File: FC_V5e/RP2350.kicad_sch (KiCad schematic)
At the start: 34 parts, among them U11 W25Q128JVS, U18 RP2350_60QFN, U5 APS1604M-3SQR-SN_C18214056, Y1 ABM8-272-T3

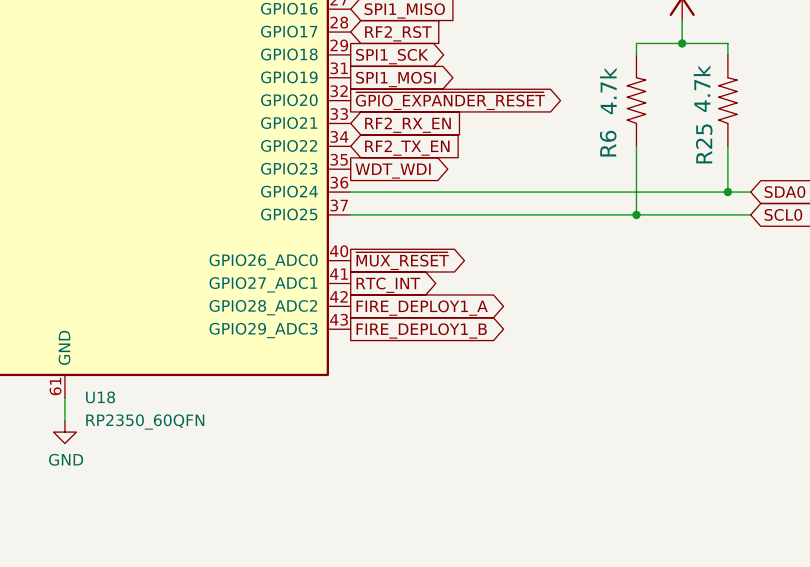
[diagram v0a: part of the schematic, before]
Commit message: Added RV3032 to Schematic
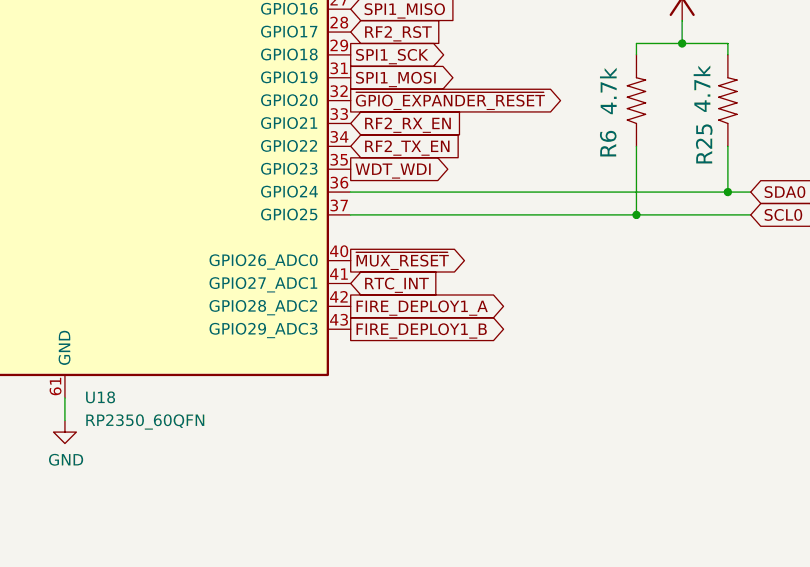
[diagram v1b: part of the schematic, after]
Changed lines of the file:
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@@
 	)
 	(global_label "RTC_INT"
-		(shape output)
+		(shape input)
 		(at 209.55 143.51 0)
 		(fields_autoplaced yes)

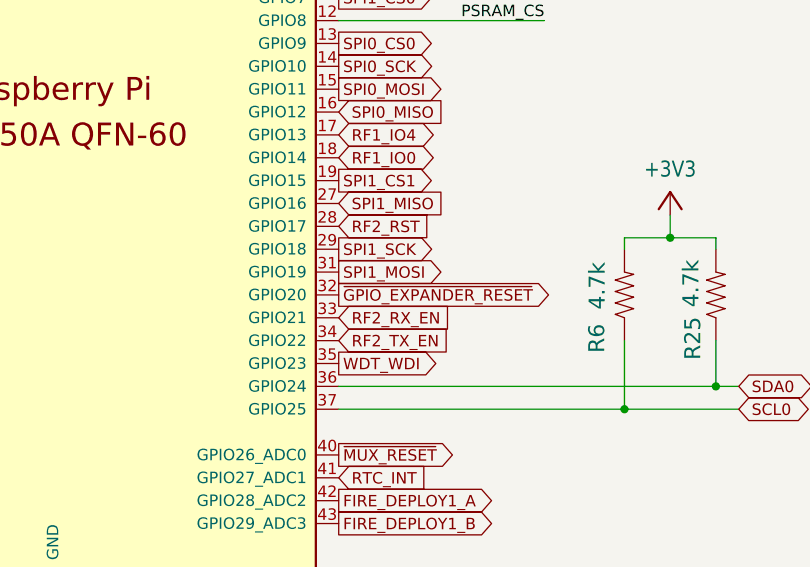
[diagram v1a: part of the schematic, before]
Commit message: Removed RF2: E28-2G4M27S
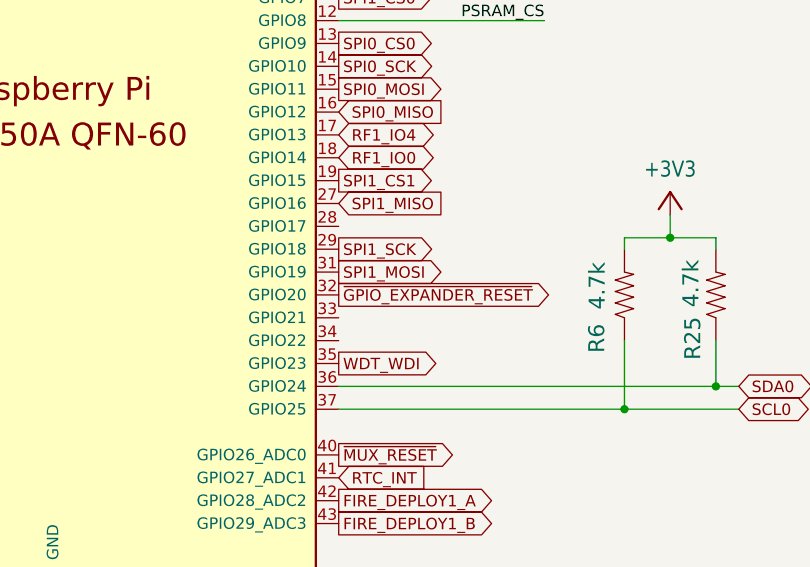
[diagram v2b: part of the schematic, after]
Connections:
- net RF2_RST: no longer names the net of U18.28 (GPIO17)
- net RF2_RX_EN: no longer names the net of U18.33 (GPIO21)
- net RF2_TX_EN: no longer names the net of U18.34 (GPIO22)
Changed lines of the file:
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@@
-		)
-	)
-	(global_label "RF2_TX_EN"
-		(shape input)
-		(at 209.55 128.27 0)
-		(fields_autoplaced yes)
-		(effects
-			(font
-				(size 1.27 1.27)
-			)
-			(justify left)
-		)
-		(property "Intersheetrefs" "${INTERSHEET_REFS}"
-			(at 222.6951 128.27 0)
-			(effects
-				(font
-					(size 1.27 1.27)
-				)
-				(justify left)
-				(hide yes)
-			)
-		)
-	)
-	(global_label "RF2_RST"
-		(shape input)
-		(at 209.55 115.57 0)
-		(fields_autoplaced yes)
-		(effects
-			(font
-				(size 1.27 1.27)
-			)
-			(justify left)
-		)
-		(property "Intersheetrefs" "${INTERSHEET_REFS}"
-			(at 220.518 115.57 0)
-			(effects
-				(font
-					(size 1.27 1.27)
-				)
-				(justify left)
-				(hide yes)
-			)
 		)
 	)
@@
 			(effects
 				(font
-					(size 1.27 1.27)
-				)
-				(justify left)
-				(hide yes)
-			)
-		)
-	)
-	(global_label "RF2_RX_EN"
-		(shape input)
-		(at 209.55 125.73 0)
-		(fields_autoplaced yes)
-		(effects
-			(font
-				(size 1.27 1.27)
-			)
-			(justify left)
-		)
-		(property "Intersheetrefs" "${INTERSHEET_REFS}"
-			(at 222.9975 125.73 0)
-			(effects
-				(font

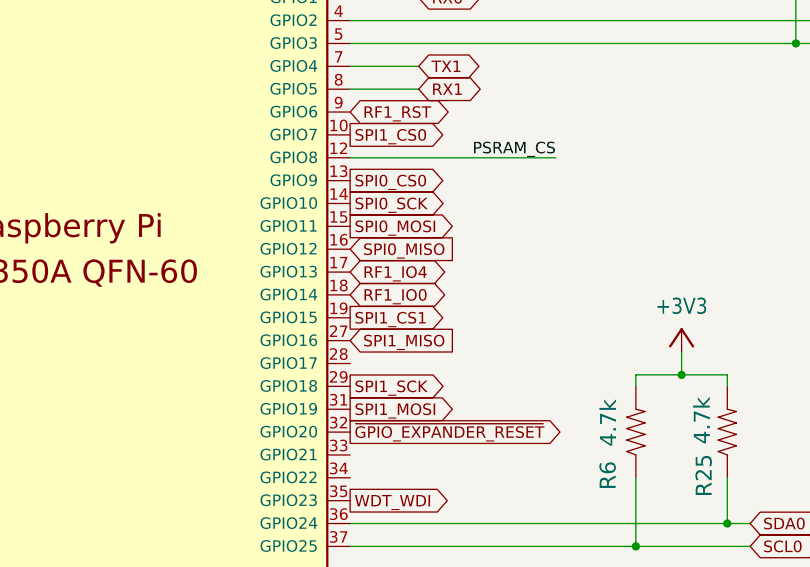
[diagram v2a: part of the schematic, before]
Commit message: Created NiceRF LR1121 Symbol and Footprint
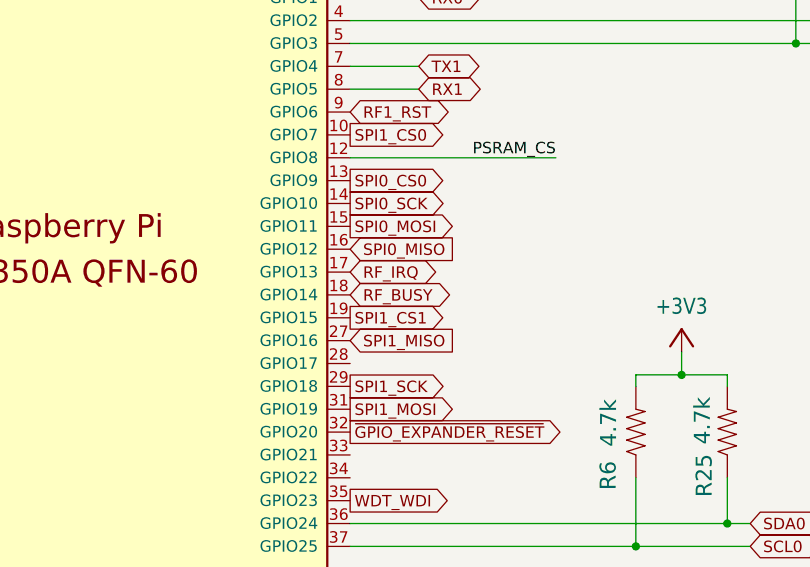
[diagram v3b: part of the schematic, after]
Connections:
- net RF1_IO0 renamed RF_BUSY
- net RF1_IO4 renamed RF_IRQ
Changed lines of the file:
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@@
 		)
 	)
-	(global_label "RF1_IO4"
+	(global_label "RF_IRQ"
 		(shape bidirectional)
 		(at 209.55 105.41 0)
@@
 		)
 		(property "Intersheetrefs" "${INTERSHEET_REFS}"
-			(at 139.7 -36.83 0)
-			(effects
-				(font
-					(size 1.27 1.27)
-				)
+			(at 220.178 105.41 0)
+			(effects
+				(font
+					(size 1.27 1.27)
+				)
+				(justify left)
 				(hide yes)
 			)
@@
 		)
 	)
-	(global_label "RF1_IO0"
+	(global_label "RF_BUSY"
 		(shape bidirectional)
 		(at 209.55 107.95 0)
@@
 		)
 		(property "Intersheetrefs" "${INTERSHEET_REFS}"
-			(at 243.84 257.81 0)
-			(effects
-				(font
-					(size 1.27 1.27)
-				)
-				(hide yes)
-			)
+			(at 221.8713 107.95 0)
+			(effects
+				(font
+					(size 1.27 1.27)
+				)
+				(justify left)
+				(hide yes)
+			)

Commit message: Fixed Vias?
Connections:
- net RF1_RST: now also U18.15 (GPIO11); no longer U18.9 (GPIO6)
- net RF_BUSY: no longer U18.18 (GPIO14)
- net RF_IRQ: now also U18.14 (GPIO10); no longer U18.17 (GPIO13)
- net SPI0_CS0: now also U18.17 (GPIO13); no longer U18.13 (GPIO9)
- net SPI0_MOSI: now also U18.19 (GPIO15); no longer U18.15 (GPIO11)
- net SPI0_SCK: now also U18.18 (GPIO14); no longer U18.14 (GPIO10)
- net SPI1_CS1: no longer U18.19 (GPIO15)
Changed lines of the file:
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@@
+	(wire
+		(pts
+			(xy 241.3 97.79) (xy 209.55 97.79)
+		)
+		(stroke
+			(width 0)
+			(type default)
+		)
+	)
 	(wire
 		(pts
@@
 		)
 	)
+	(global_label "RF1_RST"
+		(shape bidirectional)
+		(at 209.55 100.33 0)
+		(fields_autoplaced yes)
+		(effects
+			(font
+				(size 1.27 1.27)
+			)
+			(justify left)
+		)
+		(property "Intersheetrefs" "${INTERSHEET_REFS}"
+			(at 219.946 100.4094 0)
+			(effects
+				(font
+					(size 1.27 1.27)
+				)
+				(justify left)
+				(hide yes)
+			)
+		)
+	)
+	(global_label "RF_BUSY"
+		(shape bidirectional)
+		(at 241.3 101.6 0)
+		(fields_autoplaced yes)
+		(effects
+			(font
+				(size 1.27 1.27)
+			)
+			(justify left)
+		)
+		(property "Intersheetrefs" "${INTERSHEET_REFS}"
+			(at 253.6213 101.6 0)
+			(effects
+				(font
+					(size 1.27 1.27)
+				)
+				(justify left)
+				(hide yes)
+			)
+		)
+	)
 	(global_label "RTC_INT"
 		(shape input)
@@
 		)
 	)
-	(global_label "RF_IRQ"
-		(shape bidirectional)
-		(at 209.55 105.41 0)
-		(fields_autoplaced yes)
-		(effects
-			(font
-				(size 1.27 1.27)
-			)
-			(justify left)
-		)
-		(property "Intersheetrefs" "${INTERSHEET_REFS}"
-			(at 220.178 105.41 0)
-			(effects
-				(font
-					(size 1.27 1.27)
-				)
-				(justify left)
-				(hide yes)
-			)
-		)
-	)
 	(global_label "FIRE_DEPLOY1_A"
 		(shape output)
@@
 		)
 	)
-	(global_label "SPI1_CS1"
-		(shape output)
-		(at 209.55 110.49 0)
-		(fields_autoplaced yes)
-		(effects
-			(font
-				(size 1.27 1.27)
-			)
-			(justify left)
-		)
-		(property "Intersheetrefs" "${INTERSHEET_REFS}"
-			(at 221.4856 110.49 0)
-			(effects
-				(font
-					(size 1.27 1.27)
-				)
-				(justify left)
-				(hide yes)
-			)
-		)
-	)
 	(global_label "USB_DM"
 		(shape input)
@@
 		)
 	)
+	(global_label "SPI0_CS0"
+		(shape output)
+		(at 209.55 105.41 0)
+		(fields_autoplaced yes)
+		(effects
+			(font
+				(size 1.27 1.27)
+			)
+			(justify left)
+		)
+		(property "Intersheetrefs" "${INTERSHEET_REFS}"
+			(at 221.4062 105.41 0)
+			(effects
+				(font
+					(size 1.27 1.27)
+				)
+				(justify left)
+				(hide yes)
+			)
+		)
+	)
 	(global_label "SWDIO"
 		(shape input)
@@
 		)
 	)
+	(global_label "SPI0_MOSI"
+		(shape output)
+		(at 209.55 110.49 0)
+		(fields_autoplaced yes)
+		(effects
+			(font
+				(size 1.27 1.27)
+			)
+			(justify left)
+		)
+		(property "Intersheetrefs" "${INTERSHEET_REFS}"
+			(at 222.3134 110.49 0)
+			(effects
+				(font
+					(size 1.27 1.27)
+				)
+				(justify left)
+				(hide yes)
+			)
+		)
+	)
 	(global_label "RX0"
 		(shape bidirectional)
@@
 		)
 	)
-	(global_label "RF_BUSY"
-		(shape bidirectional)
-		(at 209.55 107.95 0)
-		(fields_autoplaced yes)
-		(effects
-			(font
-				(size 1.27 1.27)
-			)
-			(justify left)
-		)
-		(property "Intersheetrefs" "${INTERSHEET_REFS}"
-			(at 221.8713 107.95 0)
-			(effects
-				(font
-					(size 1.27 1.27)
-				)
-				(justify left)
-				(hide yes)
-			)
-		)
-	)
 	(global_label "FC_RESET"
 		(shape bidirectional)
@@
 		)
 	)
+	(global_label "RF_IRQ"
+		(shape bidirectional)
+		(at 241.3 97.79 0)
+		(fields_autoplaced yes)
+		(effects
+			(font
+				(size 1.27 1.27)
+			)
+			(justify left)
+		)
+		(property "Intersheetrefs" "${INTERSHEET_REFS}"
+			(at 251.928 97.79 0)
+			(effects
+				(font
+					(size 1.27 1.27)
+				)
+				(justify left)
+				(hide yes)
+			)
+		)
+	)
+	(global_label "SPI1_CS1"
+		(shape output)
+		(at 241.3 93.98 0)
+		(fields_autoplaced yes)
+		(effects
+			(font
+				(size 1.27 1.27)
+			)
+			(justify left)
+		)
+		(property "Intersheetrefs" "${INTERSHEET_REFS}"
+			(at 253.2356 93.98 0)
+			(effects
+				(font
+					(size 1.27 1.27)
+				)
+				(justify left)
+				(hide yes)
+			)
+		)
+	)
 	(global_label "TX0"
 		(shape bidirectional)
@@
 		)
 	)
-	(global_label "SPI0_CS0"
+	(global_label "SPI0_SCK"
 		(shape output)
-		(at 209.55 95.25 0)
-		(fields_autoplaced yes)
-		(effects
-			(font
-				(size 1.27 1.27)
-			)
-			(justify left)
-		)
-		(property "Intersheetrefs" "${INTERSHEET_REFS}"
-			(at 221.4062 95.25 0)
+		(at 209.55 107.95 0)
+		(fields_autoplaced yes)
+		(effects
+			(font
+				(size 1.27 1.27)
+			)
+			(justify left)
+		)
+		(property "Intersheetrefs" "${INTERSHEET_REFS}"
+			(at 221.4667 107.95 0)
 			(effects
 				(font
@@
 		)
 	)
-	(global_label "SPI0_MOSI"
-		(shape output)
-		(at 209.55 100.33 0)
-		(fields_autoplaced yes)
-		(effects
-			(font
-				(size 1.27 1.27)
-			)
-			(justify left)
-		)
-		(property "Intersheetrefs" "${INTERSHEET_REFS}"
-			(at 222.3134 100.33 0)
-			(effects
-				(font
-					(size 1.27 1.27)
-				)
-				(justify left)
-				(hide yes)
-			)
-		)
-	)
 	(global_label "FIRE_DEPLOY1_B"
 		(shape output)
@@
 		)
 	)
-	(global_label "SPI0_SCK"
-		(shape output)
-		(at 209.55 97.79 0)
-		(fields_autoplaced yes)
-		(effects
-			(font
-				(size 1.27 1.27)
-			)
-			(justify left)
-		)
-		(property "Intersheetrefs" "${INTERSHEET_REFS}"
-			(at 221.4667 97.79 0)
-			(effects
-				(font
-					(size 1.27 1.27)
-				)
-				(justify left)
-				(hide yes)
-			)
-		)
-	)
 	(global_label "SPI1_CS0"
 		(shape output)
@@
 			(effects
 				(font
-					(size 1.27 1.27)
-				)
-				(justify left)
-				(hide yes)
-			)
-		)
-	)
-	(global_label "RF1_RST"
-		(shape bidirectional)
-		(at 209.55 87.63 0)
-		(fields_autoplaced yes)
-		(effects
-			(font
-				(size 1.27 1.27)
-			)
-			(justify left)
-		)
-		(property "Intersheetrefs" "${INTERSHEET_REFS}"
-			(at 219.946 87.7094 0)
-			(effects
-				(font

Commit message: Renamed V5d Rev 3 to V5e
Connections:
- net RF_IRQ is gone; now on net SPI0_SCK: U18.14 (GPIO10)
- net RF1_RST: now also U18.9 (GPIO6); no longer U18.15 (GPIO11)
- net SPI0_CS0: now also U18.13 (GPIO9); no longer U18.17 (GPIO13)
- net SPI0_MOSI: now also U18.15 (GPIO11); no longer U18.19 (GPIO15)
- net SPI0_SCK: no longer U18.18 (GPIO14)
- net SPI1_CS1: now also U18.19 (GPIO15)
- net RF2_RST: now reaches U18.28 (GPIO17)
- net RF1_TX_EN: now reaches U18.33 (GPIO21)
- net RF1_RX_EN: now reaches U18.34 (GPIO22)
- new net RF1_IO0: U18.17 (GPIO13)
- new net RF1_IO1: U18.18 (GPIO14)
